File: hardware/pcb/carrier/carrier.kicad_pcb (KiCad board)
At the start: 2 copper layers, 66 x 54 mm, 38 parts

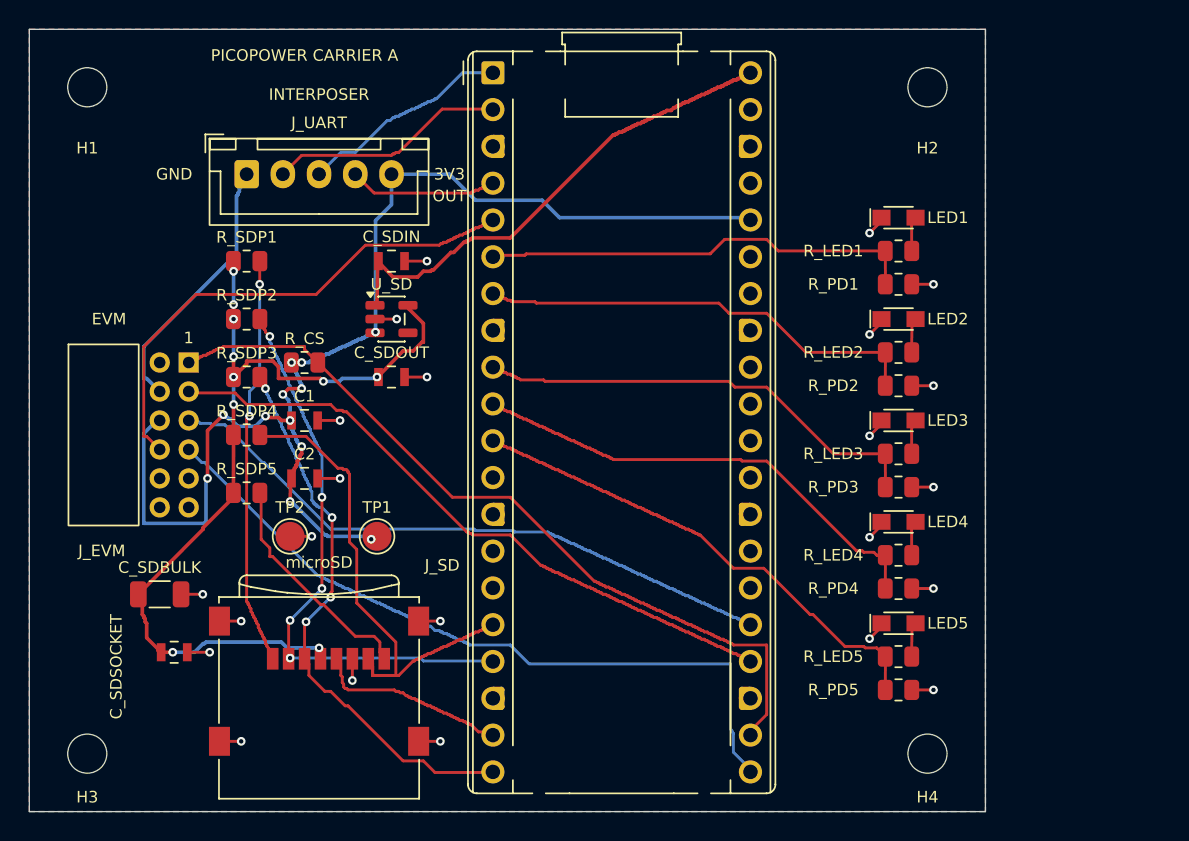
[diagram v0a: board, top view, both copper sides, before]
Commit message: Replace INA229EVM with an on-board INA229 on the carrier
- Carrier carries U_PM (INA229AIDGSR, VSSOP-10), 100 nF bypass, ALERT
  pull-up and a JST-XH sense connector J_SENSE (same pinout as interposer
  J3); the EVM socket and its footprint are removed.
- Carrier outline grows from 66 to 78 x 54 mm to make room.
- INA229 SPI0 moves to GP4-GP7 and the LEDs to GP27/26/22/21/20 so no
  trace crosses the Pico; ALERT stays on GP3.
- Carrier PWR_FLAGs added; source checks and tests updated for the new
  measurement boundary (sense nets only on J_SENSE and U_PM).
- BOM, assembly review, passive selections, checklist (new sense-ic row,
  carrier mock-up reset to pending), footprint review and docs updated.
- INA229 pad geometry compared with the TI DGS0010A example land pattern.
- Add project-state handoff note. Interposer and carrier fabrication
  gates remain open; nothing is released.

make carrier-build does not currently reproduce the routed board; the saved
carrier.kicad_pcb is the source of truth (see the carrier README).

Co-Authored-By: Claude Sonnet 5.5 <noreply@anthropic.com>
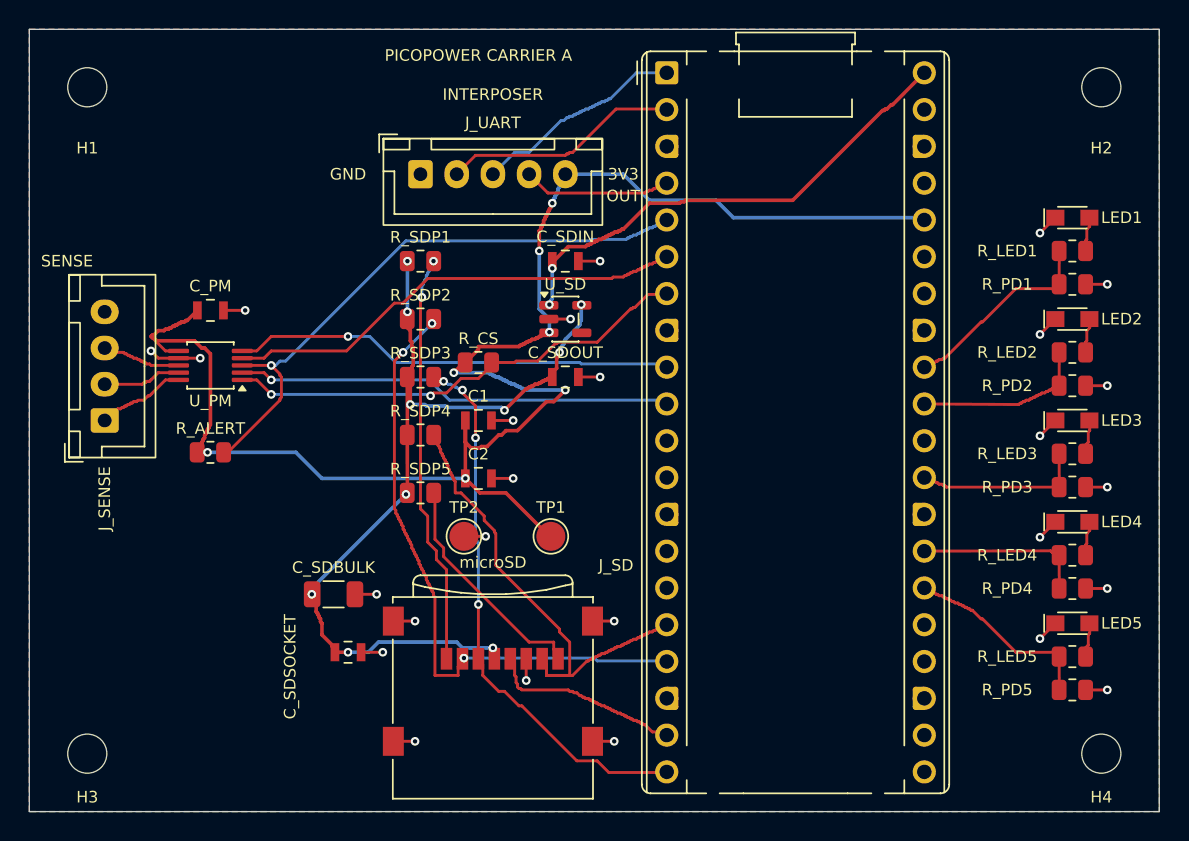
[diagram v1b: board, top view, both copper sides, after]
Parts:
- removed J_EVM: INA229EVM / direct plug, Carrier:NPPN062FJFN
- added C_PM: 100nF X7R 16V, Carrier:C_0805_Murata, F.Cu at (12.5, 19.4)
- added J_SENSE: INTERPOSER SENSE / JST-XH-4, Carrier:XH4, F.Cu at (5.20, 27.0)
- added R_ALERT: 10k 1%, Carrier:R_0805, F.Cu at (12.5, 29.2)
- added U_PM: INA229 power monitor, Carrier:VSSOP10, F.Cu at (12.5, 23.2)
- moved C1 12.0 mm to (31.0, 27.0)
- moved C2 12.0 mm to (31.0, 31.0)
- moved C_SDBULK 12.0 mm to (21.0, 39.0)
- moved C_SDIN 12.0 mm to (37.0, 16.0)
- moved C_SDOUT 12.0 mm to (37.0, 24.0)
- moved C_SDSOCKET 12.0 mm to (22.0, 43.0)
- moved D1 12.0 mm to (72.0, 13.0)
- moved D2 12.0 mm to (72.0, 20.0)
- moved D3 12.0 mm to (72.0, 27.0)
- moved D4 12.0 mm to (72.0, 34.0)
- moved D5 12.0 mm to (72.0, 41.0)
- moved H2 12.0 mm to (74.0, 4.00)
- moved H4 12.0 mm to (74.0, 50.0)
- moved J_PICO 12.0 mm to (44.0, 3.00)
- moved J_SD 12.0 mm to (32.0, 45.0)
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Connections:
- J_PICO pad 10: /LED4_GPIO -> /MOSI
- J_PICO pad 11: /LED5_GPIO -> unconnected-(J_PICO-NC-Pad11)
- J_PICO pad 21: /MISO -> unconnected-(J_PICO-NC-Pad21)
- J_PICO pad 22: /CS -> unconnected-(J_PICO-NC-Pad22)
- J_PICO pad 24: /SCLK -> unconnected-(J_PICO-NC-Pad24)
- J_PICO pad 25: /MOSI -> unconnected-(J_PICO-NC-Pad25)
- J_PICO pad 26: unconnected-(J_PICO-NC-Pad26) -> /LED5_GPIO
- J_PICO pad 27: unconnected-(J_PICO-NC-Pad27) -> /LED4_GPIO
- J_PICO pad 29: unconnected-(J_PICO-NC-Pad29) -> /LED3_GPIO
- J_PICO pad 31: unconnected-(J_PICO-NC-Pad31) -> /LED2_GPIO
- J_PICO pad 32: unconnected-(J_PICO-NC-Pad32) -> /LED1_GPIO
- J_PICO pad 6: /LED1_GPIO -> /MISO
- J_PICO pad 7: /LED2_GPIO -> /CS
- J_PICO pad 9: /LED3_GPIO -> /SCLK
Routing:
- net /PICO_3V3: track 89.5 -> 113.4 mm, vias 12 -> 7
- net /CS: track 55.7 -> 32.9 mm, vias 0 -> 2
- net /LED5_GPIO: track 35.6 -> 13.6 mm
- net /LED4_GPIO: track 33.7 -> 11.8 mm
- net /LED3_GPIO: track 31.9 -> 11.9 mm
- net /MISO: track 51.7 -> 32.2 mm
- net /LED2_GPIO: track 31.1 -> 12.2 mm
- net /LED1_GPIO: track 30.2 -> 14.0 mm
- net /SCLK: track 46.5 -> 30.6 mm, vias 0 -> 1
- net /MOSI: track 44.7 -> 30.3 mm, vias 0 -> 1
- net /GND: track 53.0 -> 39.6 mm, vias 23 -> 26
- net /SENSE_PLUS: track 0.00 -> 6.26 mm
- net /ALERT: track 35.4 -> 41.6 mm, vias 0 -> 1
- net /SENSE_VBUS: track 0.00 -> 5.60 mm
- net /SENSE_MINUS: track 0.00 -> 5.43 mm
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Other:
- board size 66 x 54 mm -> 78 x 54 mm
- board text added: "SENSE"
- board text removed: "EVM"

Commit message: Turn the carrier microSD socket 180 degrees and reroute its nets
The owner asked for the socket to face the other way so the card is easier to
insert. Only the seven SD signal nets were rerouted (grid router, J_SD nets
only), ground pad 6 got a via, and the microSD label moved below the body.
Native DRC: 0 violations, 0 unconnected; ERC and parity unchanged. Release rows
restamped; the JLCPCB viewer check for J_SD must be repeated.

Co-Authored-By: Claude Sonnet 5.5 <noreply@anthropic.com>
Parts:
- turned J_SD to 180 degrees
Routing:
- net /SD_3V3: track 61.7 -> 68.0 mm
- net /SD_MOSI: track 38.2 -> 44.4 mm
- net /SD_DAT2: track 28.6 -> 34.5 mm
- net /SD_MISO: track 34.7 -> 40.1 mm, vias 0 -> 3
- net /GND: track 39.6 -> 41.1 mm, vias 26 -> 27
- net /SD_CS: track 44.1 -> 42.7 mm, vias 3 -> 4
- net /SD_DAT1: track 16.0 -> 14.7 mm
- net /SD_SCLK: track 13.9 -> 14.6 mm
